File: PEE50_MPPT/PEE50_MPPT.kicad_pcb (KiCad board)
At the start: 2 copper layers, 100 x 100 mm, 172 parts, among them J1 Vout, J2 Conn_01x02_Female, J3 Conn_01x02_Female, J4 Conn_01x03_Female, J5 PV_IN1, J6 PV_IN1, J7 PV_IN1, J8 PV_IN1, Q1 BC547, Q2 BC547, Q3 BC547, Q4 BC547, U1 LM3480-3.3, U10 NTA4151PT1G, U11 CSD18514Q5A, U12 CSD18543Q3A, U13 TPS552882QRPMRQ1, U14 MAX44284FAUT+T, U15 MAX44284FAUT+T, U16 NTA4151PT1G, U17 CSD18514Q5A, U18 CSD18543Q3A, U19 TPS552882QRPMRQ1, U2 MSP430FR2353TDBT, U20 MAX44284FAUT+T, U21 MAX44284FAUT+T, U22 NTA4151PT1G, U23 CSD18514Q5A, U24 CSD18543Q3A, U25 TPS552882QRPMRQ1, U26 MAX44284FAUT+T, U27 MAX44284FAUT+T, U3 ADG706BRUZ, U4 NTA4151PT1G, U5 CSD18514Q5A, U6 CSD18543Q3A, U7 TPS552882QRPMRQ1, U8 MAX44284FAUT+T, U9 MAX44284FAUT+T

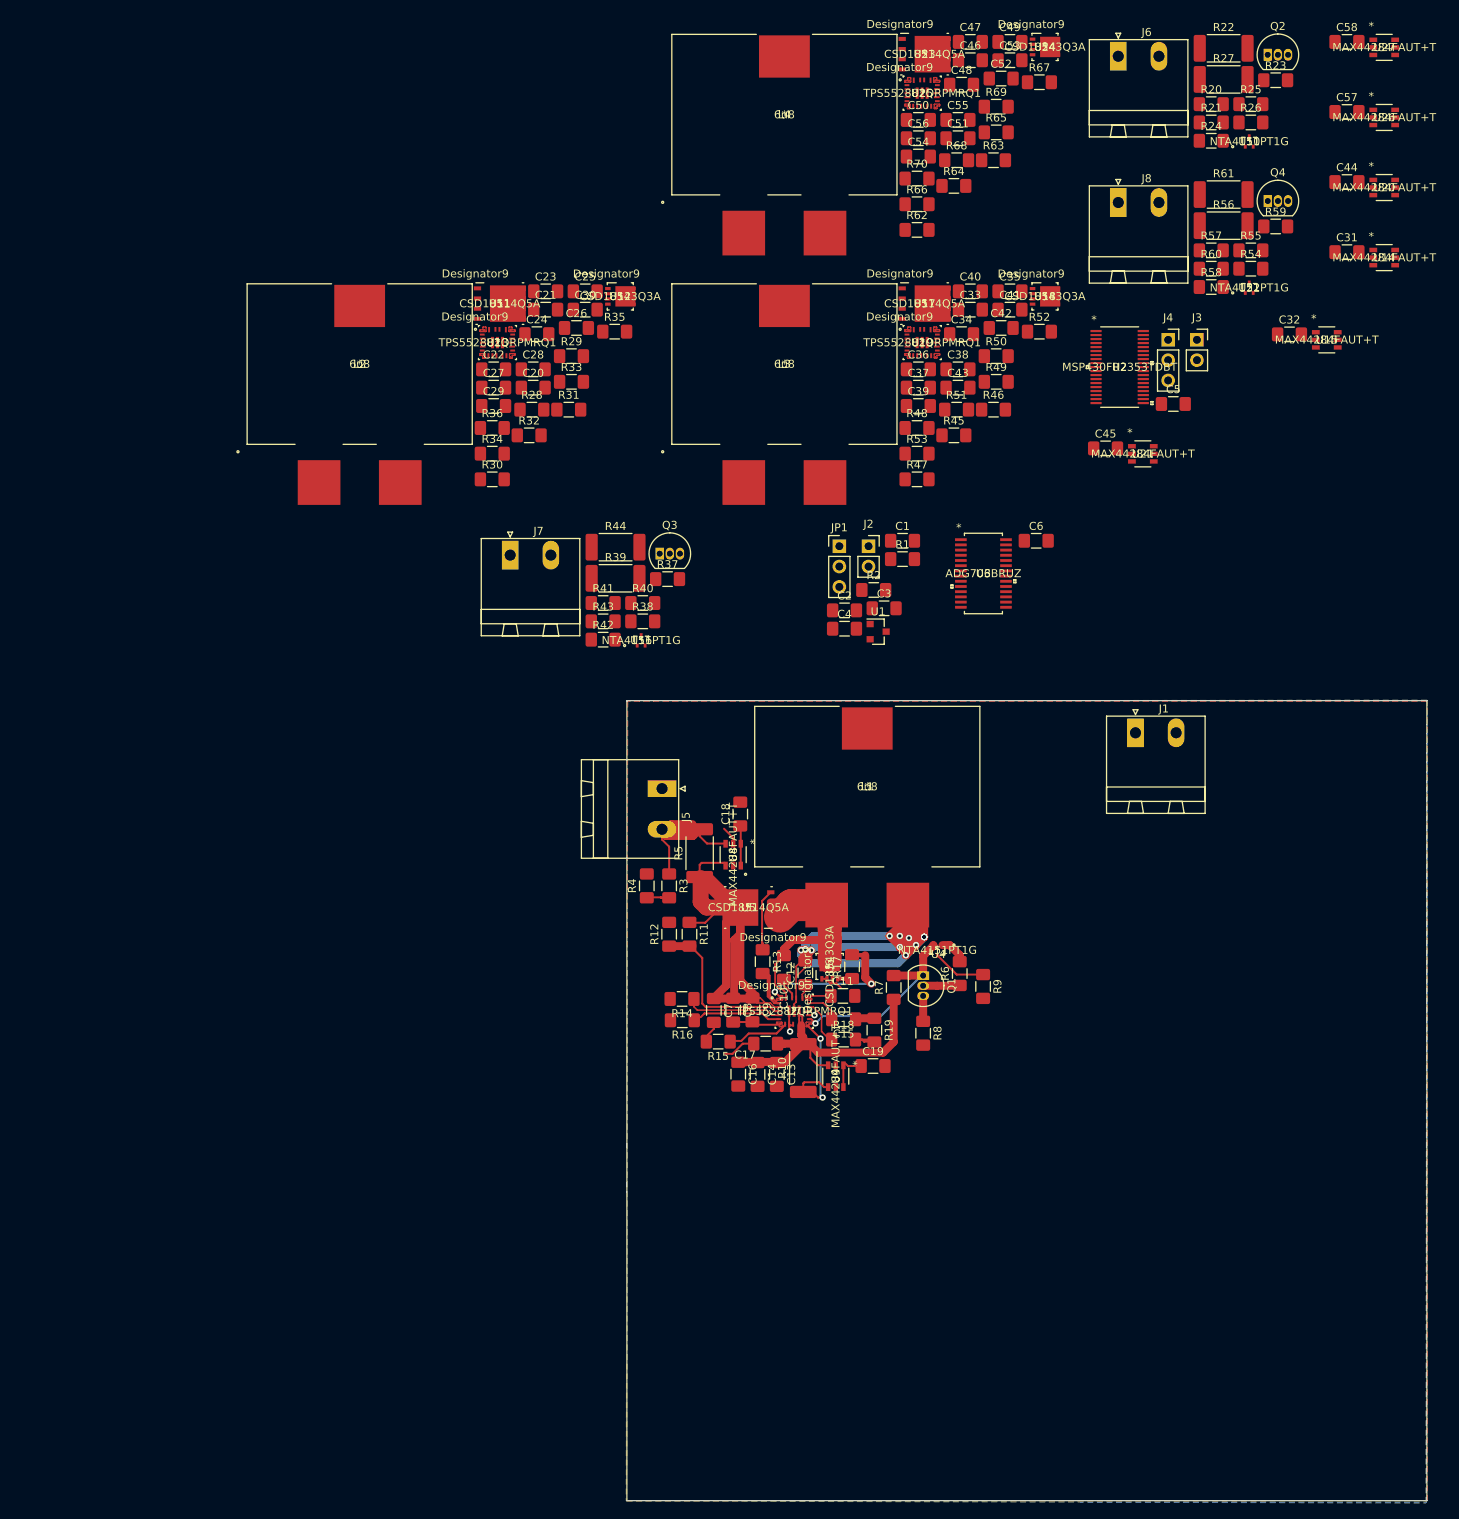
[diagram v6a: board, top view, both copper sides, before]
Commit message: 4 mppt's klaar en geplaatst
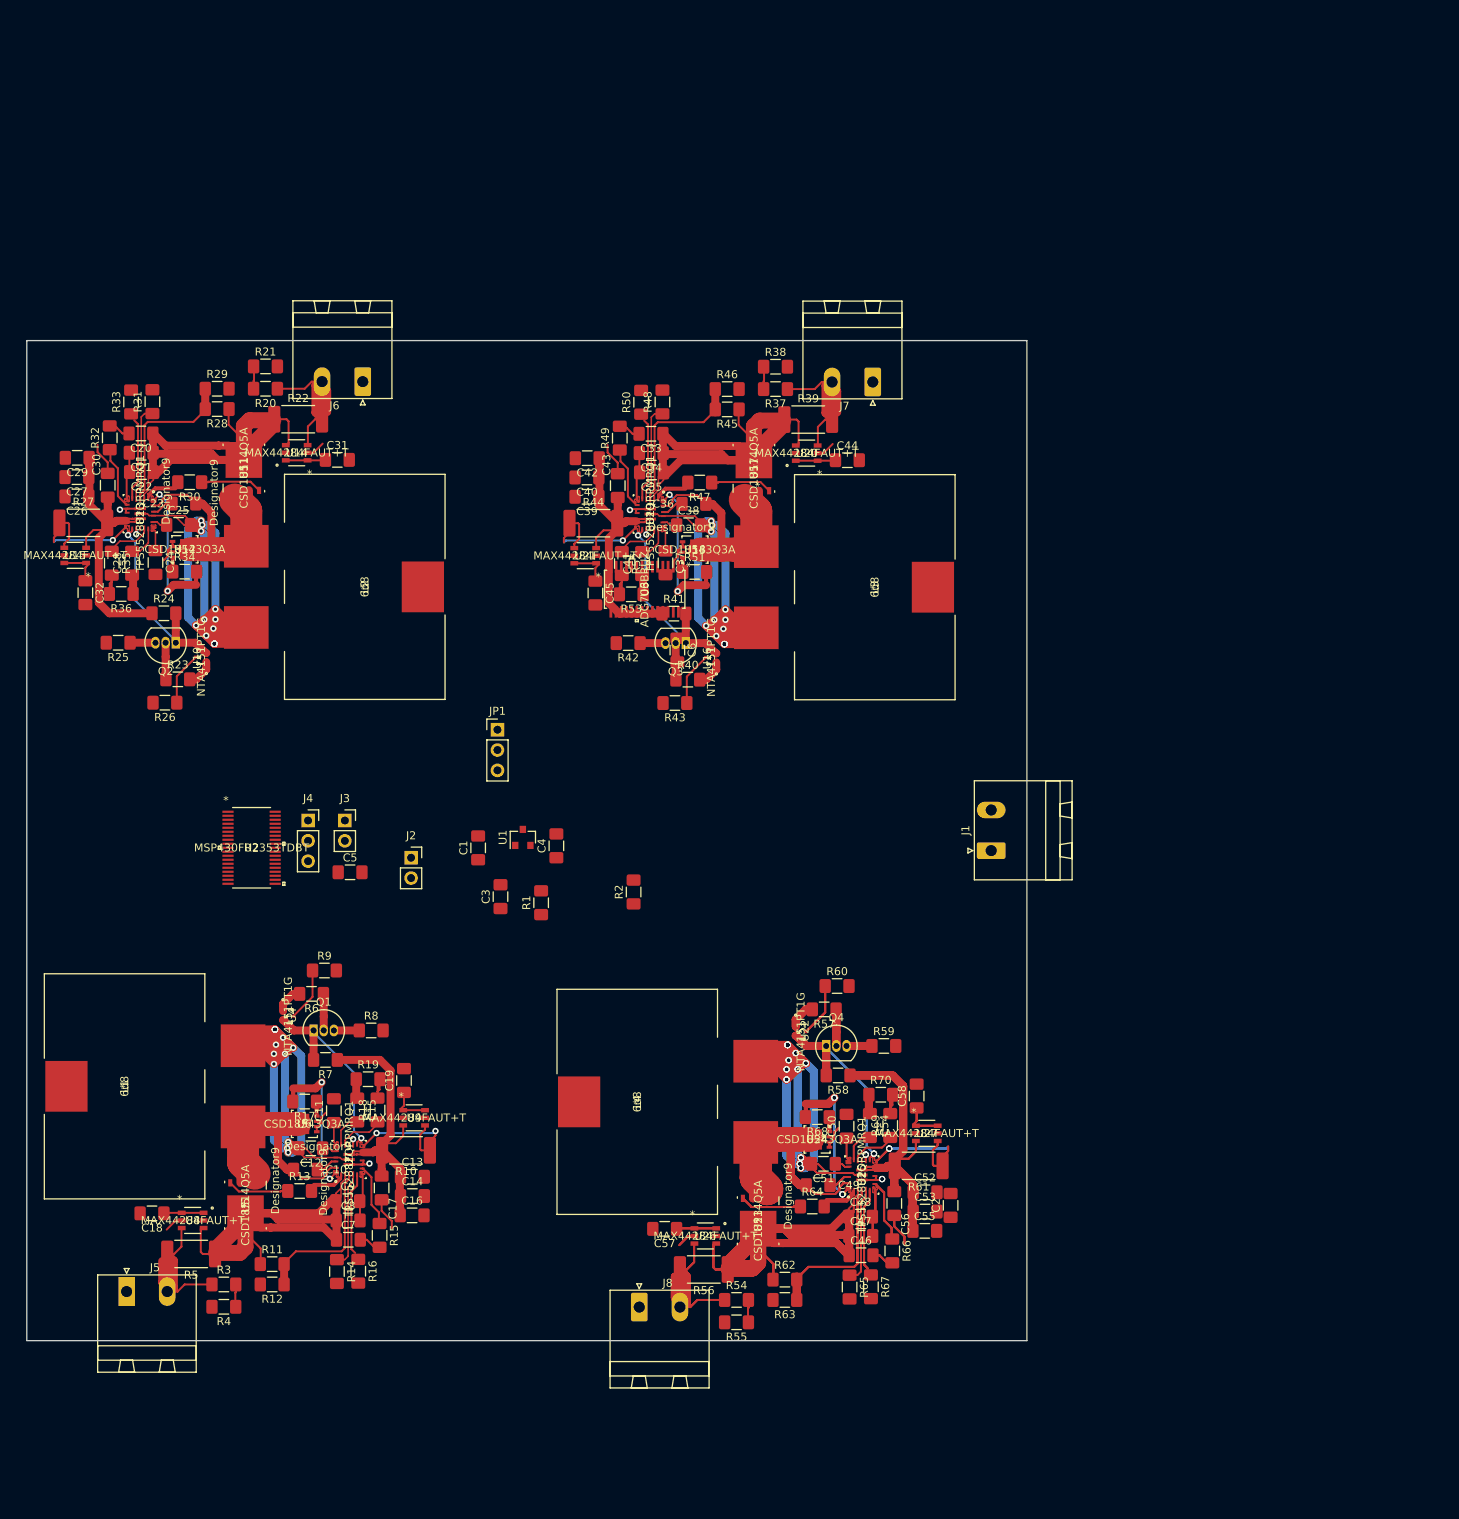
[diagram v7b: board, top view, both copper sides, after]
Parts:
- moved C57 163.6 mm to (104.7, 166.0), turned to 180 degrees
- moved U26 163.6 mm to (109.8, 166.9)
- moved U15 158.7 mm to (31.0, 81.8), turned to 180 degrees
- moved R25 156.8 mm to (36.4, 92.8), turned to 180 degrees
- moved R23 156.3 mm to (43.9, 97.3)
- moved Q2 155.0 mm to (43.6, 92.8), turned to 180 degrees
- moved C32 153.9 mm to (32.3, 86.5), turned to 270 degrees
- moved R26 153.9 mm to (42.3, 100.3), turned to 180 degrees
- moved R27 152.9 mm to (32.1, 77.8)
- moved R67 152.0 mm to (130.5, 173.3), turned to 270 degrees
- moved J8 150.5 mm to (101.5, 175.8)
- moved C46 150.0 mm to (129.3, 169.3)
- moved C47 149.9 mm to (129.2, 166.9)
- moved R55 148.6 mm to (113.7, 177.7), turned to 180 degrees
- moved U23 147.3 mm to (116.4, 165.0), turned to 270 degrees
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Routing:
- net Net-(C51-Pad2): track 0.00 -> 189.4 mm, vias 0 -> 28
- net /sheet609F5795/sheet609C6964/PVin+: track 0.00 -> 138.4 mm
- net Pgnd: track 27.1 -> 135.3 mm, vias 2 -> 10
- net Net-(C25-Pad2): track 0.00 -> 94.7 mm, vias 0 -> 14
- net Net-(C38-Pad2): track 0.00 -> 94.7 mm, vias 0 -> 14
- net /sheet609F5795/sheet609C6964/ISP: track 0.00 -> 79.7 mm
- net /sheet609F4756/sheet609C6964/PVin+: track 0.00 -> 69.2 mm
- net /sheet609F26BA/sheet609C6964/PVin+: track 0.00 -> 69.2 mm
- net /Sheet609B465C/Vout: track 15.6 -> 78.2 mm, vias 2 -> 6
- net Net-(C49-Pad1): track 0.00 -> 59.6 mm
- net /sheet609F5795/sheet609C6964/FB: track 0.00 -> 57.5 mm, vias 0 -> 2
- net /sheet609F5795/sheet609C6965/R+: track 0.00 -> 48.0 mm
- net Net-(R62-Pad2): track 0.00 -> 46.8 mm
- net /sheet609F4756/sheet609C6964/ISP: track 0.00 -> 39.9 mm
- net /sheet609F26BA/sheet609C6964/ISP: track 0.00 -> 39.9 mm
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- removed copper zone on B.Cu, net Pgnd
- removed copper zone on F.Cu, net Pgnd
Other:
- board size 100 x 100 mm -> 125 x 125 mm

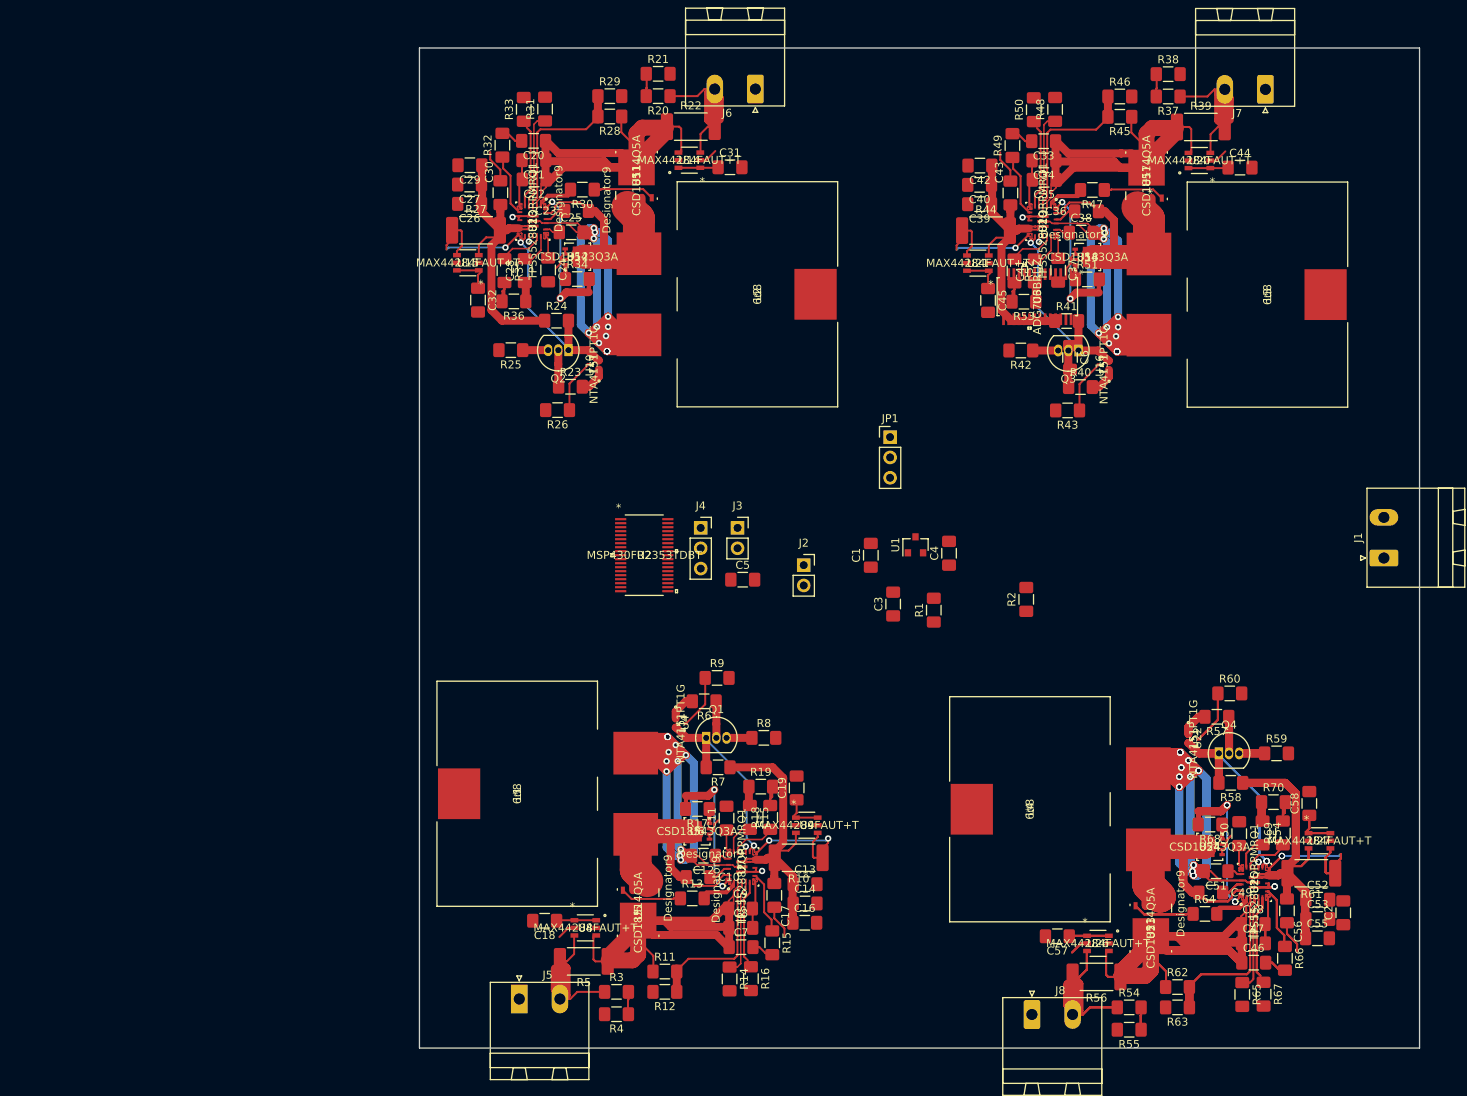
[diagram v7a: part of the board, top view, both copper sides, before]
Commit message: power banen gerout, locatie toegewezen voor uC
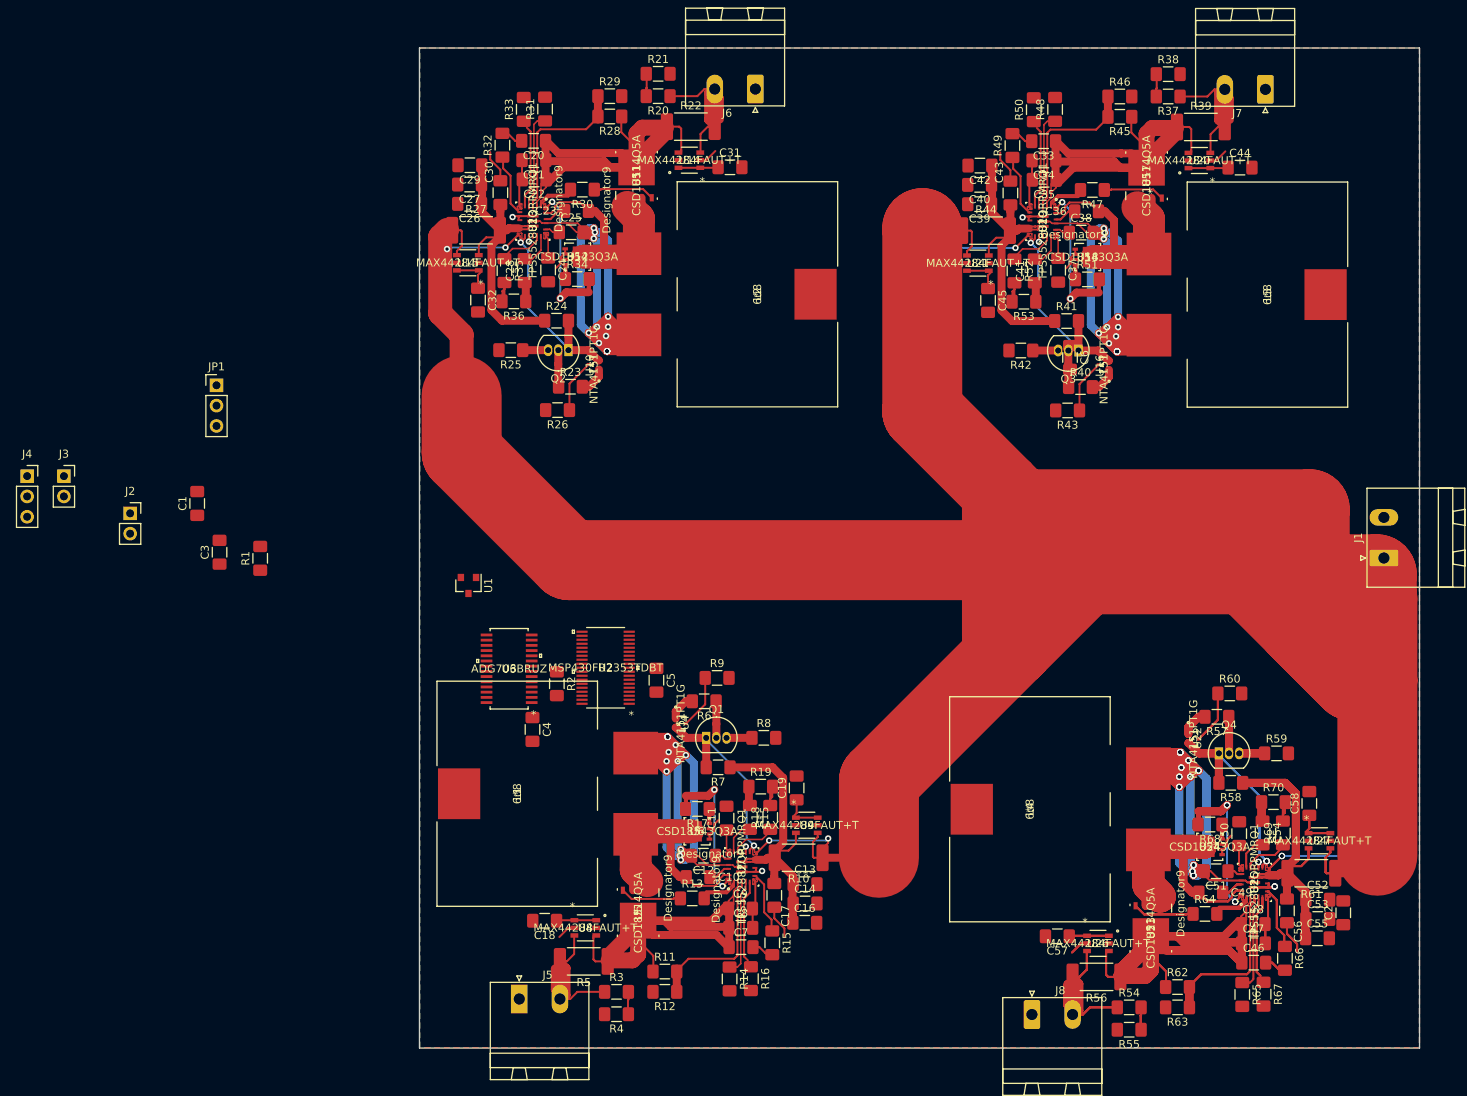
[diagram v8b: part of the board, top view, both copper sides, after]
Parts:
- moved J2 84.4 mm to (-11.2, 113.2)
- moved J4 84.4 mm to (-24.1, 108.5)
- moved R1 84.4 mm to (5.08, 118.8)
- moved C1 84.4 mm to (-2.79, 111.9)
- moved C3 84.4 mm to (0.00, 118.0)
- moved J3 84.4 mm to (-19.5, 108.5)
- moved JP1 84.4 mm to (-0.38, 97.2)
- moved U3 80.8 mm to (36.2, 132.6), turned to 180 degrees
- moved R2 59.6 mm to (42.2, 134.5), turned to 270 degrees
- moved C4 56.5 mm to (39.1, 140.2), turned to 270 degrees
- moved U1 56.1 mm to (31.1, 122.2), turned to 270 degrees
- moved C5 16.6 mm to (54.6, 134.0), turned to 270 degrees
- moved U2 14.9 mm to (48.3, 132.5), turned to 180 degrees
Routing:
- net /Sheet609B465C/Vout: track 78.2 -> 482.8 mm, vias 6 -> 7
- added copper zone on B.Cu, net Pgnd
- added copper zone on F.Cu, net Pgnd
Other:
- net class power: trace_width 0.25 -> 10
